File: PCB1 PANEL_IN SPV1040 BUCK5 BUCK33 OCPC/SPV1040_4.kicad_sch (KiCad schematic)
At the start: 14 parts, among them J5 SOLAR, U5 SPV1040TTR

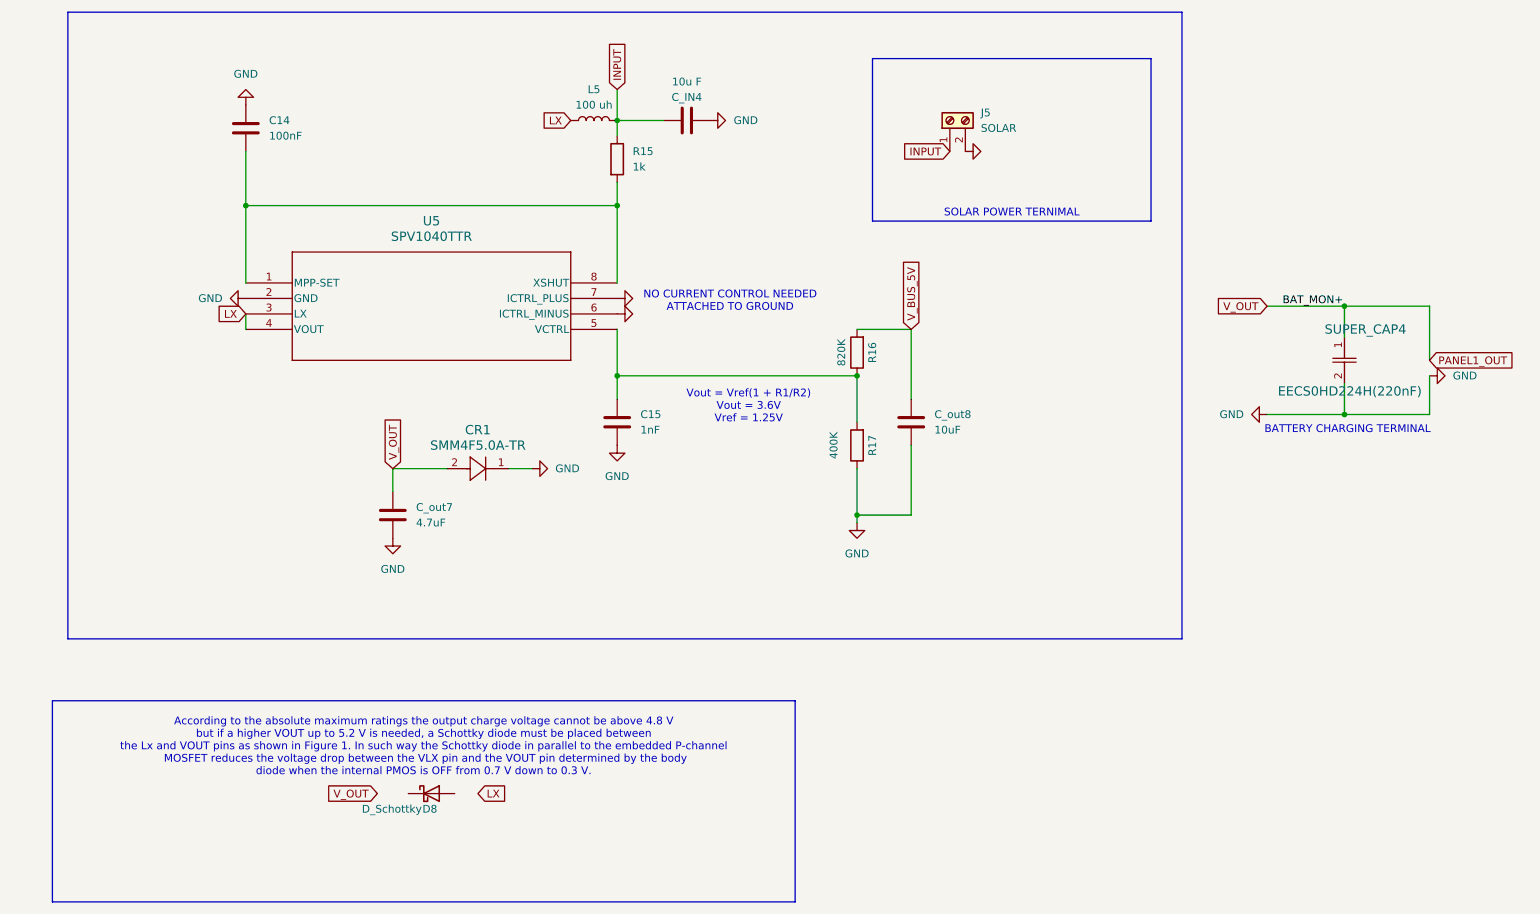
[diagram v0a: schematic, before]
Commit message: Relabeling according to standards
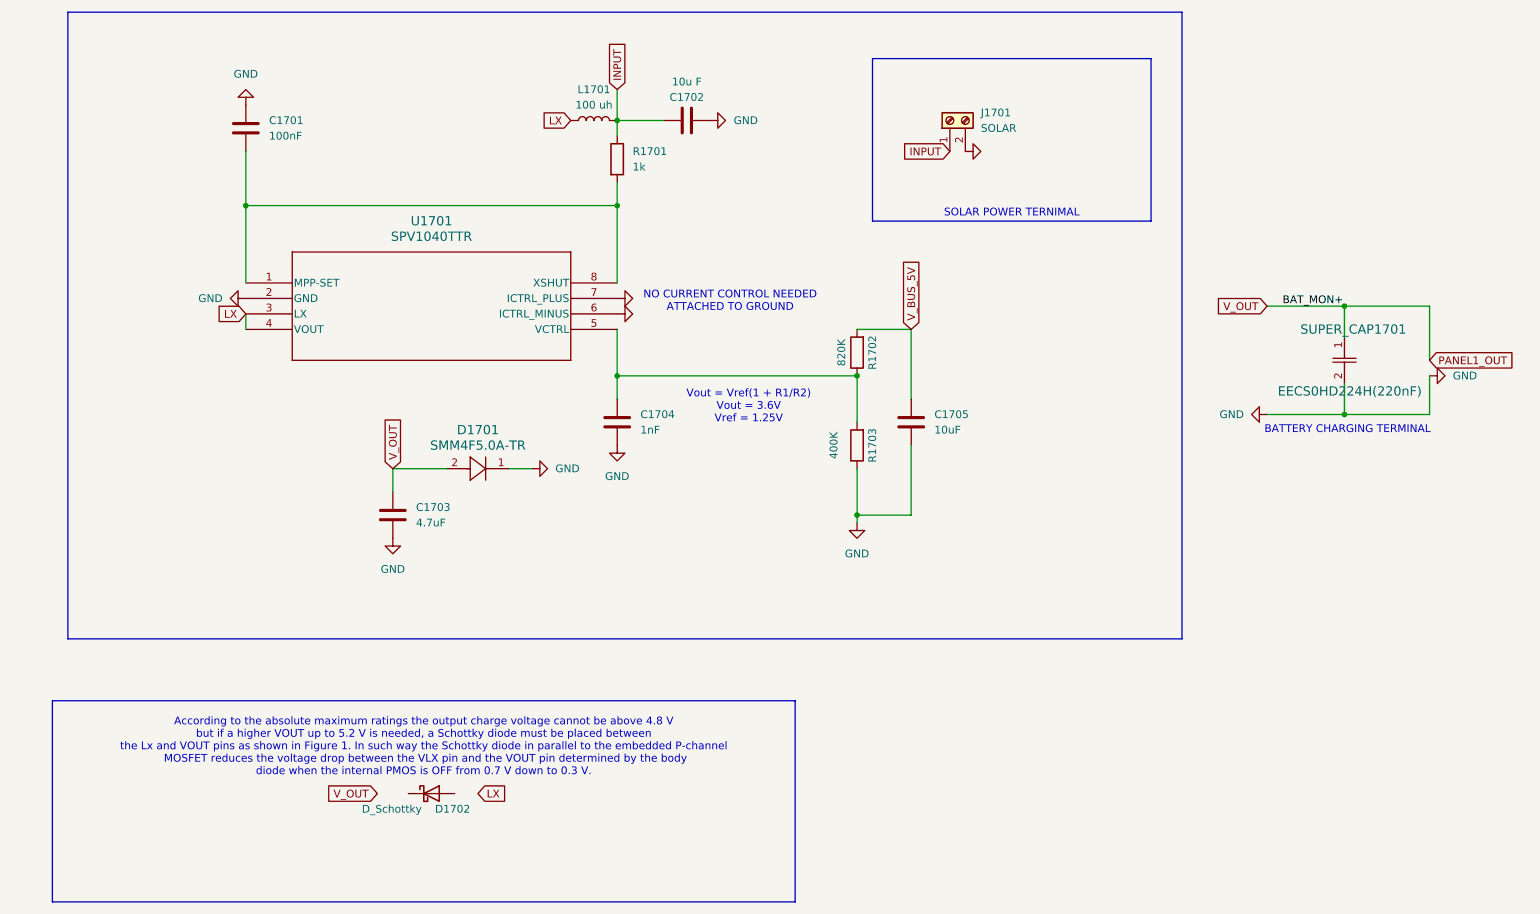
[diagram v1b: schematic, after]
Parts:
- D1701: renamed from CR1; footprint CR_F5.0A-TR_STM -> (none)
- renumbered C14 to C1701, C_IN4 to C1702, C_out7 to C1703, C15 to C1704, C_out8 to C1705, D8 to D1702, J5 to J1701, L5 to L1701, R15 to R1701, R16 to R1702, R17 to R1703, SUPER_CAP4 to SUPER_CAP1701, U5 to U1701
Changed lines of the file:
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@@
 		(on_board yes)
 		(dnp no)
-		(property "Reference" "SUPER_CAP4"
+		(property "Reference" "SUPER_CAP1701"
 			(at 241.3 82.55 90)
 			(effects
@@
 			(project "PCB1 PANEL_IN SPV1040 BUCK5 BUCK33 OCPC"
 				(path "/494c9d9f-6b33-4248-a813-27ffaaa929bd/2771644a-42c1-4e74-9e93-0ffcf5523547"
-					(reference "SUPER_CAP4")
+					(reference "SUPER_CAP1701")
 					(unit 1)
 				)
@@
 		(dnp no)
 		(fields_autoplaced yes)
-		(property "Reference" "C14"
+		(property "Reference" "C1701"
 			(at 54.61 48.2599 0)
 			(effects
@@
 			(project "PCB1 PANEL_IN SPV1040 BUCK5 BUCK33 OCPC"
 				(path "/494c9d9f-6b33-4248-a813-27ffaaa929bd/2771644a-42c1-4e74-9e93-0ffcf5523547"
-					(reference "C14")
+					(reference "C1701")
 					(unit 1)
 				)
@@
 		(on_board yes)
 		(dnp no)
-		(property "Reference" "R16"
+		(property "Reference" "R1702"
 			(at 153.67 86.36 90)
 			(effects
@@
 			(project "PCB1 PANEL_IN SPV1040 BUCK5 BUCK33 OCPC"
 				(path "/494c9d9f-6b33-4248-a813-27ffaaa929bd/2771644a-42c1-4e74-9e93-0ffcf5523547"
-					(reference "R16")
+					(reference "R1702")
 					(unit 1)
 				)
@@
 		(on_board yes)
 		(dnp no)
-		(property "Reference" "D8"
-			(at 82.2326 161.29 0)
+		(property "Reference" "D1702"
+			(at 87.63 161.29 0)
 			(effects
 				(font
@@
 			(project "PCB1 PANEL_IN SPV1040 BUCK5 BUCK33 OCPC"
 				(path "/494c9d9f-6b33-4248-a813-27ffaaa929bd/2771644a-42c1-4e74-9e93-0ffcf5523547"
-					(reference "D8")
+					(reference "D1702")
 					(unit 1)
 				)
@@
 		(on_board yes)
 		(dnp no)
-		(property "Reference" "C_IN4"
+		(property "Reference" "C1702"
 			(at 123.19 44.45 90)
 			(effects
@@
 			(project "PCB1 PANEL_IN SPV1040 BUCK5 BUCK33 OCPC"
 				(path "/494c9d9f-6b33-4248-a813-27ffaaa929bd/2771644a-42c1-4e74-9e93-0ffcf5523547"
-					(reference "C_IN4")
+					(reference "C1702")
 					(unit 1)
 				)
@@
 		(on_board yes)
 		(dnp no)
-		(property "Reference" "R17"
+		(property "Reference" "R1703"
 			(at 153.67 101.6 90)
 			(effects
@@
 			(project "PCB1 PANEL_IN SPV1040 BUCK5 BUCK33 OCPC"
 				(path "/494c9d9f-6b33-4248-a813-27ffaaa929bd/2771644a-42c1-4e74-9e93-0ffcf5523547"
-					(reference "R17")
+					(reference "R1703")
 					(unit 1)
 				)
@@
 		(dnp no)
 		(fields_autoplaced yes)
-		(property "Reference" "J5"
+		(property "Reference" "J1701"
 			(at 171.45 46.9899 90)
 			(effects
@@
 			(project "PCB1 PANEL_IN SPV1040 BUCK5 BUCK33 OCPC"
 				(path "/494c9d9f-6b33-4248-a813-27ffaaa929bd/2771644a-42c1-4e74-9e93-0ffcf5523547"
-					(reference "J5")
+					(reference "J1701")
 					(unit 1)
 				)
@@
 		(dnp no)
 		(fields_autoplaced yes)
-		(property "Reference" "C_out8"
+		(property "Reference" "C1705"
 			(at 163.83 96.5199 0)
 			(effects
@@
 			(project "PCB1 PANEL_IN SPV1040 BUCK5 BUCK33 OCPC"
 				(path "/494c9d9f-6b33-4248-a813-27ffaaa929bd/2771644a-42c1-4e74-9e93-0ffcf5523547"
-					(reference "C_out8")
+					(reference "C1705")
 					(unit 1)
 				)
@@
 		(dnp no)
 		(fields_autoplaced yes)
-		(property "Reference" "L5"
+		(property "Reference" "L1701"
 			(at 107.95 43.18 90)
 			(effects
@@
 			(project "PCB1 PANEL_IN SPV1040 BUCK5 BUCK33 OCPC"
 				(path "/494c9d9f-6b33-4248-a813-27ffaaa929bd/2771644a-42c1-4e74-9e93-0ffcf5523547"
-					(reference "L5")
+					(reference "L1701")
 					(unit 1)
 				)
@@
 		(dnp no)
 		(fields_autoplaced yes)
-		(property "Reference" "CR1"
+		(property "Reference" "D1701"
 			(at 88.9 99.06 0)
 			(effects
@@
 			)
 		)
-		(property "Footprint" "CR_F5.0A-TR_STM"
+		(property "Footprint" ""
 			(at 83.82 105.41 0)
 			(effects
@@
 			(project ""
 				(path "/494c9d9f-6b33-4248-a813-27ffaaa929bd/2771644a-42c1-4e74-9e93-0ffcf5523547"
-					(reference "CR1")
+					(reference "D1701")
 					(unit 1)
 				)
@@
 		(dnp no)
 		(fields_autoplaced yes)
-		(property "Reference" "R15"
+		(property "Reference" "R1701"
 			(at 114.3 53.3399 0)
 			(effects
@@
 			(project "PCB1 PANEL_IN SPV1040 BUCK5 BUCK33 OCPC"
 				(path "/494c9d9f-6b33-4248-a813-27ffaaa929bd/2771644a-42c1-4e74-9e93-0ffcf5523547"
-					(reference "R15")
+					(reference "R1701")
 					(unit 1)
 				)
@@
 		(dnp no)
 		(fields_autoplaced yes)
-		(property "Reference" "U5"
+		(property "Reference" "U1701"
 			(at 81.28 64.77 0)
 			(effects
@@
 			(project "PCB1 PANEL_IN SPV1040 BUCK5 BUCK33 OCPC"
 				(path "/494c9d9f-6b33-4248-a813-27ffaaa929bd/2771644a-42c1-4e74-9e93-0ffcf5523547"
-					(reference "U5")
+					(reference "U1701")
 					(unit 1)
 				)
@@
 		(dnp no)
 		(fields_autoplaced yes)
-		(property "Reference" "C15"
+		(property "Reference" "C1704"
 			(at 115.57 96.5199 0)
 			(effects
@@
 			(project "PCB1 PANEL_IN SPV1040 BUCK5 BUCK33 OCPC"
 				(path "/494c9d9f-6b33-4248-a813-27ffaaa929bd/2771644a-42c1-4e74-9e93-0ffcf5523547"
-					(reference "C15")
+					(reference "C1704")
 					(unit 1)
 				)
@@
 		(dnp no)
 		(fields_autoplaced yes)
-		(property "Reference" "C_out7"
+		(property "Reference" "C1703"
 			(at 78.74 111.7599 0)
 			(effects
@@
 			(project "PCB1 PANEL_IN SPV1040 BUCK5 BUCK33 OCPC"
 				(path "/494c9d9f-6b33-4248-a813-27ffaaa929bd/2771644a-42c1-4e74-9e93-0ffcf5523547"
-					(reference "C_out7")
-					(unit 1)
-				)
+					(reference "C1703")
+					(unit 1)
+				)
